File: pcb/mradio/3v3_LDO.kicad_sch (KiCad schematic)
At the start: 13 parts, among them U202 TPS7A8500ARGRR

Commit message: Fixed passives
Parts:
- renumbered C201 to C101, C204 to C102, C207 to C103, C208 to C104, C209 to C105, C216 to C106, C219 to C107, C220 to C108, C221 to C109, C222 to C110, D201 to D101, R209 to R101, U202 to U101
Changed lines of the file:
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@@
 		(dnp no)
 		(fields_autoplaced yes)
-		(property "Reference" "#PWR0207"
+		(property "Reference" "#PWR0102"
 			(at 85.09 87.63 0)
 			(hide yes)
@@
 			(project "power_distribution"
 				(path "/e6698048-9125-4cf3-9b80-868e7e50deb6/cd16224c-c66f-4bd7-8549-cc0e165ba672"
-					(reference "#PWR0207")
+					(reference "#PWR0102")
 					(unit 1)
 				)
@@
 		(dnp no)
 		(fields_autoplaced yes)
-		(property "Reference" "#PWR0212"
+		(property "Reference" "#PWR0105"
 			(at 148.59 107.95 0)
 			(hide yes)
@@
 			(project "power_distribution"
 				(path "/e6698048-9125-4cf3-9b80-868e7e50deb6/cd16224c-c66f-4bd7-8549-cc0e165ba672"
-					(reference "#PWR0212")
+					(reference "#PWR0105")
 					(unit 1)
 				)
@@
 		(dnp no)
 		(fields_autoplaced yes)
-		(property "Reference" "C219"
+		(property "Reference" "C107"
 			(at 165.1 71.1199 0)
 			(show_name no)
@@
 			(project "power_distribution"
 				(path "/e6698048-9125-4cf3-9b80-868e7e50deb6/cd16224c-c66f-4bd7-8549-cc0e165ba672"
-					(reference "C219")
+					(reference "C107")
 					(unit 1)
 				)
@@
 		(dnp no)
 		(fields_autoplaced yes)
-		(property "Reference" "C209"
+		(property "Reference" "C105"
 			(at 95.25 83.8199 0)
 			(show_name no)
@@
 			(project "power_distribution"
 				(path "/e6698048-9125-4cf3-9b80-868e7e50deb6/cd16224c-c66f-4bd7-8549-cc0e165ba672"
-					(reference "C209")
+					(reference "C105")
 					(unit 1)
 				)
@@
 		(dnp no)
 		(fields_autoplaced yes)
-		(property "Reference" "R209"
+		(property "Reference" "R101"
 			(at 167.64 54.61 90)
 			(show_name no)
@@
 			(project "power_distribution"
 				(path "/e6698048-9125-4cf3-9b80-868e7e50deb6/cd16224c-c66f-4bd7-8549-cc0e165ba672"
-					(reference "R209")
+					(reference "R101")
 					(unit 1)
 				)
@@
 		(dnp no)
 		(fields_autoplaced yes)
-		(property "Reference" "#PWR0203"
+		(property "Reference" "#PWR0101"
 			(at 63.5 76.2 0)
 			(hide yes)
@@
 			(project "power_distribution"
 				(path "/e6698048-9125-4cf3-9b80-868e7e50deb6/cd16224c-c66f-4bd7-8549-cc0e165ba672"
-					(reference "#PWR0203")
+					(reference "#PWR0101")
 					(unit 1)
 				)
@@
 		(dnp no)
 		(fields_autoplaced yes)
-		(property "Reference" "#PWR0215"
+		(property "Reference" "#PWR0106"
 			(at 161.29 85.09 0)
 			(hide yes)
@@
 			(project "power_distribution"
 				(path "/e6698048-9125-4cf3-9b80-868e7e50deb6/cd16224c-c66f-4bd7-8549-cc0e165ba672"
-					(reference "#PWR0215")
+					(reference "#PWR0106")
 					(unit 1)
 				)
@@
 		(dnp no)
 		(fields_autoplaced yes)
-		(property "Reference" "#PWR0208"
+		(property "Reference" "#PWR0103"
 			(at 91.44 95.25 0)
 			(hide yes)
@@
 			(project "power_distribution"
 				(path "/e6698048-9125-4cf3-9b80-868e7e50deb6/cd16224c-c66f-4bd7-8549-cc0e165ba672"
-					(reference "#PWR0208")
+					(reference "#PWR0103")
 					(unit 1)
 				)
@@
 		(dnp no)
 		(fields_autoplaced yes)
-		(property "Reference" "D201"
+		(property "Reference" "D101"
 			(at 183.1975 53.34 0)
 			(show_name no)
@@
 			(project "power_distribution"
 				(path "/e6698048-9125-4cf3-9b80-868e7e50deb6/cd16224c-c66f-4bd7-8549-cc0e165ba672"
-					(reference "D201")
+					(reference "D101")
 					(unit 1)
 				)
@@
 		(dnp no)
 		(fields_autoplaced yes)
-		(property "Reference" "C221"
+		(property "Reference" "C109"
 			(at 189.23 71.1199 0)
 			(show_name no)
@@
 			(project "power_distribution"
 				(path "/e6698048-9125-4cf3-9b80-868e7e50deb6/cd16224c-c66f-4bd7-8549-cc0e165ba672"
-					(reference "C221")
+					(reference "C109")
 					(unit 1)
 				)
@@
 		(dnp no)
 		(fields_autoplaced yes)
-		(property "Reference" "C201"
+		(property "Reference" "C101"
 			(at 67.31 60.9599 0)
 			(show_name no)
@@
 			(project "power_distribution"
 				(path "/e6698048-9125-4cf3-9b80-868e7e50deb6/cd16224c-c66f-4bd7-8549-cc0e165ba672"
-					(reference "C201")
+					(reference "C101")
 					(unit 1)
 				)
@@
 		(dnp no)
 		(fields_autoplaced yes)
-		(property "Reference" "C208"
+		(property "Reference" "C104"
 			(at 90.17 60.9599 0)
 			(show_name no)
@@
 			(project "power_distribution"
 				(path "/e6698048-9125-4cf3-9b80-868e7e50deb6/cd16224c-c66f-4bd7-8549-cc0e165ba672"
-					(reference "C208")
+					(reference "C104")
 					(unit 1)
 				)
@@
 		(dnp no)
 		(fields_autoplaced yes)
-		(property "Reference" "U202"
+		(property "Reference" "U101"
 			(at 128.27 48.26 0)
 			(show_name no)
@@
 			(project "power_distribution"
 				(path "/e6698048-9125-4cf3-9b80-868e7e50deb6/cd16224c-c66f-4bd7-8549-cc0e165ba672"
-					(reference "U202")
+					(reference "U101")
 					(unit 1)
 				)
@@
 		(dnp no)
 		(fields_autoplaced yes)
-		(property "Reference" "C220"
+		(property "Reference" "C108"
 			(at 177.8 71.1199 0)
 			(show_name no)
@@
 			(project "power_distribution"
 				(path "/e6698048-9125-4cf3-9b80-868e7e50deb6/cd16224c-c66f-4bd7-8549-cc0e165ba672"
-					(reference "C220")
+					(reference "C108")
 					(unit 1)
 				)
@@
 		(dnp no)
 		(fields_autoplaced yes)
-		(property "Reference" "C216"
+		(property "Reference" "C106"
 			(at 153.67 81.2799 0)
 			(show_name no)
@@
 			(project "power_distribution"
 				(path "/e6698048-9125-4cf3-9b80-868e7e50deb6/cd16224c-c66f-4bd7-8549-cc0e165ba672"
-					(reference "C216")
+					(reference "C106")
 					(unit 1)
 				)
@@
 		(dnp no)
 		(fields_autoplaced yes)
-		(property "Reference" "C204"
+		(property "Reference" "C102"
 			(at 78.74 60.9599 0)
 			(show_name no)
@@
 			(project "power_distribution"
 				(path "/e6698048-9125-4cf3-9b80-868e7e50deb6/cd16224c-c66f-4bd7-8549-cc0e165ba672"
-					(reference "C204")
+					(reference "C102")
 					(unit 1)
 				)
@@
 		(dnp no)
 		(fields_autoplaced yes)
-		(property "Reference" "C222"
+		(property "Reference" "C110"
 			(at 200.66 71.1199 0)
 			(show_name no)
@@
 			(project "power_distribution"
 				(path "/e6698048-9125-4cf3-9b80-868e7e50deb6/cd16224c-c66f-4bd7-8549-cc0e165ba672"
-					(reference "C222")
+					(reference "C110")
 					(unit 1)
 				)
@@
 		(dnp no)
 		(fields_autoplaced yes)
-		(property "Reference" "C207"
+		(property "Reference" "C103"
 			(at 88.9 76.1999 0)
 			(show_name no)
@@
 			(project "power_distribution"
 				(path "/e6698048-9125-4cf3-9b80-868e7e50deb6/cd16224c-c66f-4bd7-8549-cc0e165ba672"
-					(reference "C207")
+					(reference "C103")
 					(unit 1)
 				)
@@
 		(dnp no)
 		(fields_autoplaced yes)
-		(property "Reference" "#PWR0209"
+		(property "Reference" "#PWR0104"
 			(at 100.33 111.76 0)
 			(hide yes)
@@
 			(project "power_distribution"
 				(path "/e6698048-9125-4cf3-9b80-868e7e50deb6/cd16224c-c66f-4bd7-8549-cc0e165ba672"
-					(reference "#PWR0209")
+					(reference "#PWR0104")
 					(unit 1)
 				)
@@
 		(dnp no)
 		(fields_autoplaced yes)
-		(property "Reference" "#PWR0220"
+		(property "Reference" "#PWR0107"
 			(at 187.96 67.31 0)
 			(hide yes)
@@
 			(project "power_distribution"
 				(path "/e6698048-9125-4cf3-9b80-868e7e50deb6/cd16224c-c66f-4bd7-8549-cc0e165ba672"
-					(reference "#PWR0220")
-					(unit 1)
-				)
+					(reference "#PWR0107")
+					(unit 1)
+				)

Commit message: Voltage conversion
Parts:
- added TP5: 3v3_TP, Module:RaspberryPi_Pico_SMD, symbol Connector:TestPoint
- C109: value 1uF -> 10uF
- C110: value 0.1uF -> 10uF
- R101: value 260 -> 1.2k
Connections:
- net 3v3_LDO_OUT: now also TP5.1
- net 3.7V_Buck_out renamed 3v7_Buck_Out
- no-connect marks 0 -> 3

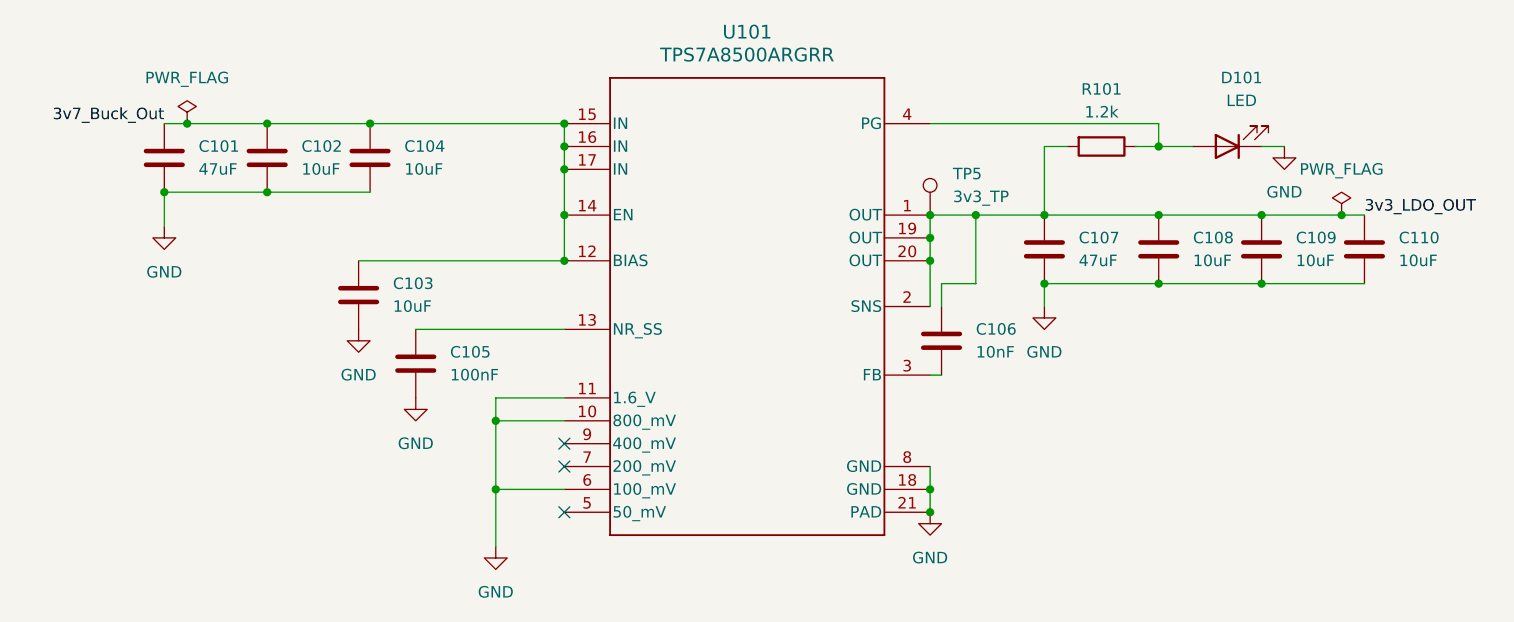
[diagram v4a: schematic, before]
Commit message: LDO footprint updates
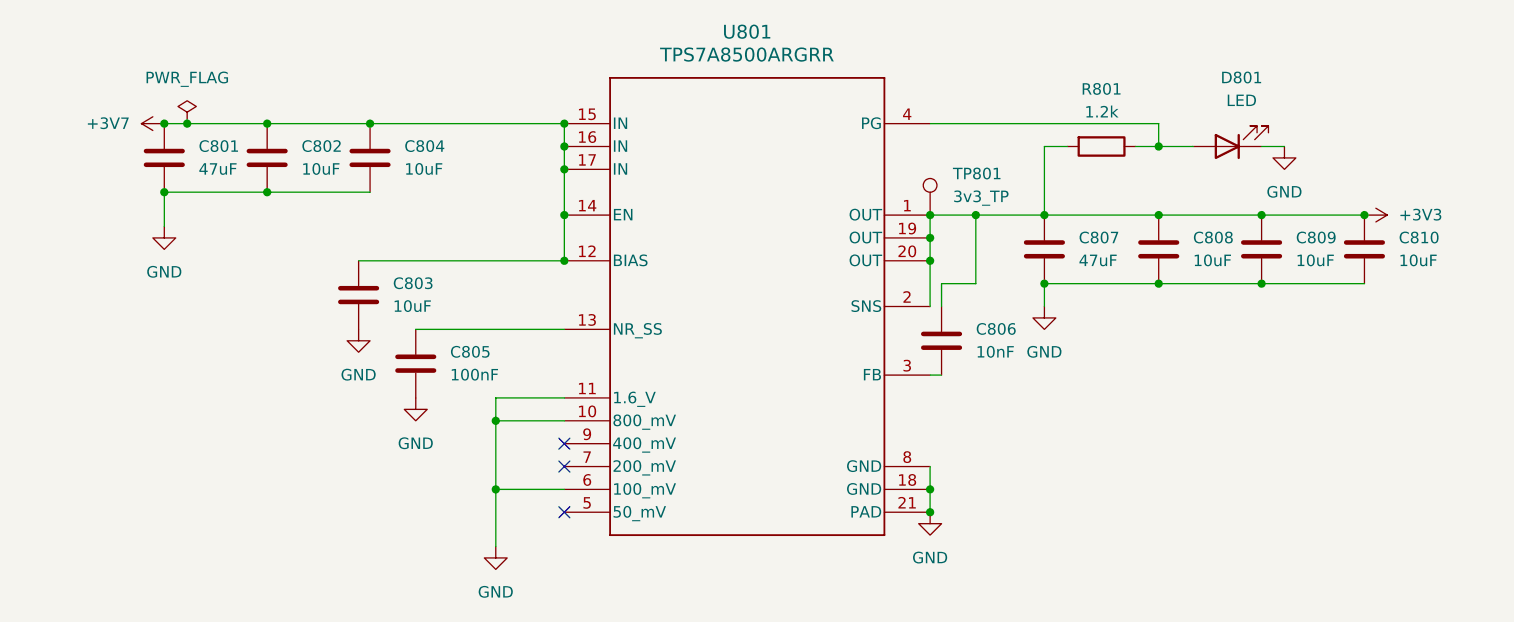
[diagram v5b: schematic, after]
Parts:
- C801: renamed from C101; footprint RGR0020A -> Capacitor_SMD:C_0603_1608Metric
- C802: renamed from C102; footprint RGR0020A -> Capacitor_SMD:C_0603_1608Metric
- C803: renamed from C103; footprint RGR0020A -> Capacitor_SMD:C_0603_1608Metric
- C804: renamed from C104; footprint RGR0020A -> Capacitor_SMD:C_0603_1608Metric
- C805: renamed from C105; footprint (none) -> Capacitor_SMD:C_0603_1608Metric
- C806: renamed from C106; footprint (none) -> Capacitor_SMD:C_0603_1608Metric
- C807: renamed from C107; footprint (none) -> Capacitor_SMD:C_0603_1608Metric
- C808: renamed from C108; footprint (none) -> Capacitor_SMD:C_0603_1608Metric
- C809: renamed from C109; footprint (none) -> Capacitor_SMD:C_0603_1608Metric
- C810: renamed from C110; footprint (none) -> Capacitor_SMD:C_0603_1608Metric
- D801: renamed from D101; footprint (none) -> LED_SMD:LED_0603_1608Metric
- R801: renamed from R101; footprint (none) -> Resistor_SMD:R_0603_1608Metric
- U801: renamed from U101; footprint RGR0020A -> TPS7A8500RGRR:RGR0020A
- renumbered TP5 to TP801
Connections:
- net 3v3_LDO_OUT renamed +3V3
- net 3v7_Buck_Out renamed +3V7

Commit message: Update some footprints
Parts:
- TP801: footprint Module:RaspberryPi_Pico_SMD -> TestPoint:TestPoint_Loop_D2.60mm_Drill0.9mm_Beaded
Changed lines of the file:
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@@
 			)
 		)
-		(property "Footprint" "Module:RaspberryPi_Pico_SMD"
+		(property "Footprint" "TestPoint:TestPoint_Loop_D2.60mm_Drill0.9mm_Beaded"
 			(at 153.67 68.58 0)
 			(hide yes)

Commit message: make test points smaller
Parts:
- TP801: footprint TestPoint:TestPoint_Loop_D2.60mm_Drill0.9mm_Beaded -> TestPoint:TestPoint_Loop_D1.80mm_Drill1.0mm_Beaded
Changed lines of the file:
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@@
 			)
 		)
-		(property "Footprint" "TestPoint:TestPoint_Loop_D2.60mm_Drill0.9mm_Beaded"
+		(property "Footprint" "TestPoint:TestPoint_Loop_D1.80mm_Drill1.0mm_Beaded"
 			(at 153.67 68.58 0)
 			(hide yes)

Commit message: all traces routed
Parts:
- U801: footprint TPS7A8500RGRR:RGR0020A -> TPS7A8500RGRR:TPS7A8500RGRR
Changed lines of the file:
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@@
 			)
 		)
-		(property "Footprint" "TPS7A8500RGRR:RGR0020A"
+		(property "Footprint" "TPS7A8500RGRR:TPS7A8500RGRR"
 			(at 128.27 78.74 0)
 			(hide yes)
